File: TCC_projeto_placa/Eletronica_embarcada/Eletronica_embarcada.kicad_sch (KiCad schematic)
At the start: 70 parts, among them J1 ST-LINK, J2 OUT_Bluepill, J3 BOOT_JUMPER, J4 BUZZER

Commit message: ATT
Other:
- note added: "ACELERÔMETRO"
- note added: "MAGNETÔMETRO"
- moved on the sheet: C1, C2, C3, C4, C6, C7, C8, C?, CON?, D?, J1, J2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

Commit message: att
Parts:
- removed C?: C, symbol Device:C
- removed C?: 100nF, Capacitor_SMD:C_0603_1608Metric_Pad1.08x0.95mm_HandSolder, symbol Device:C
- removed CON?: USB_B, Connector_USB:USB_B_Lumberg_2411_02_Horizontal, symbol Connector:USB_B
- removed J1: ST-LINK, symbol Connector_Generic:Conn_02x05_Odd_Even
- removed J2: OUT_Bluepill, symbol Connector_Generic:Conn_01x04
- removed L?: BLM21PG221SN1D, Inductor_SMD:L_0805_2012Metric, symbol pspice:INDUCTOR
- added C? (x2): 0.1uF, symbol Device:C
- added C?: C, symbol Device:C
- added C?: 470u, 16V, symbol Device:C
- added C?: 100n, symbol Device:C
- added C?: 0.01uF, symbol Device:C
- added C?: 1000u,16V, symbol Device:C
- added C?: 2200pF, symbol Device:C
- added D? (x2): LED, symbol Device:LED
- added D?: D, Diode_SMD:D_SOD-123, symbol pspice:DIODE
- added J?: OUT_Bluepill, symbol Connector_Generic:Conn_01x04
- added J?: USB Conector, symbol Connector_Generic:Conn_01x05
- added J?: BM280 I2C, symbol Connector_Generic:Conn_01x06
- added J?: MPU6050, symbol Connector_Generic:Conn_01x08
- added R? (x3): 4.7k, symbol Device:R
- added R?: 510R, symbol Device:R
- added R? (x2): 10K, Resistor_SMD:R_0603_1608Metric_Pad0.98x0.95mm_HandSolder, symbol Device:R
- added R?: 510, symbol Device:R
- added U?: MPU-6050, Sensor_Motion:InvenSense_QFN-24_4x4mm_P0.5mm, symbol Sensor_Motion:MPU-6050
- added U?: NCP1117-5.0_SOT223, Package_TO_SOT_SMD:SOT-223-3_TabPin2, symbol Regulator_Linear:NCP1117-5.0_SOT223
- C3, C4: value 12p -> 20p
- C7, C8: value 100p -> 20p
- CON?: value CR123A -> Bateria min 7V
- Q? (x2): value Q_NPN_Darlington_BCE -> MMBT6427-F
- R?: value R -> 4.7k
- R? (x2): value R -> 20R
- R? (x2): value 1K -> 10K
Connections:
- net +3V3: now also U?.6 (VDDIO), C?.1, J?.1 (Pin_1), J?.1 (Pin_1), J?.1 (Pin_1), R?.1, R?.1, R?.1; no longer R?.1
- net +5V: now also R?.1, C?.1, C?.1, J?.1 (Pin_1), U?.2 (VO); no longer C?.1, D?.2 (A), J?.2 (Pin_2), J?.2 (Pin_2), RT?.2
- net 0: now also C?.2, C?.2, C?.2, C?.2, C?.2, C?.2, C?.2, C?.2, J?.2 (Pin_2), J?.2 (Pin_2), J?.4 (Pin_4), J?.4 (Pin_4), J?.5 (Pin_5), R?.2, R?.2, U?.1 (CLKIN), U?.1 (GND), U?.11 (FSYNC), U?.18 (GND)
- net D+: now also U?.15 (USBD+), J?.3 (Pin_3)
- net D-: now also U?.16 (USBD-), J?.2 (Pin_2)
- net PIN-SCL: now also J?.3 (Pin_3)
- net PIN-SDA: now also J?.4 (Pin_4)
- net SWCLK: now also J?.3 (Pin_3)
- net SWDIO: now also J?.2 (Pin_2)
- net PC13: now reaches U?.2 (PC13)
- net PC13: now also D?.1 (K)
- net at R?.1, U?.32 (PA11): now also R?.2
- net at R?.1, U?.33 (PA12): no longer R?.2
- net at U?.5 (SDO): now also R?.1
- net VDDIO: no longer names the net of U?.2 (CSB)
- net VDDIO: now also R?.2; no longer U?.6 (VDDIO)
- new net: C?.1, U?.10 (REGOUT)
- new net: C?.1, U?.20 (CPOUT)
- new net: R?.1, U?.9 (AD0)
- new net: D?.2 (A), R?.2 (x2)
- new net: C?.1, D?.2 (A), U?.3 (VI)
- new net +3.3V: C?.1, C?.1, R?.1, R?.1, U?.13 (VDD), U?.8 (VDDIO)
- new net GND: D?.1 (K)
- new net SCL1: J?.3 (Pin_3), R?.2, U?.23 (SCL)
- new net SDA1: J?.4 (Pin_4), R?.2, U?.24 (SDA)
- new net VBAT: C?.1, D?.1 (K), D?.2 (A), J?.2 (Pin_2), J?.2 (Pin_2), RT?.2
- no-connect marks 19 -> 23
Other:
- note added: "Alimentação"
- note added: "CIRCUITO ARM-M3"
- note added: "CONECTOR BOOT"
- note added: "CONECTORES PINOS DO BLUEPILL"
- note added: "Comunicação serial/USB"
- note added: "GRAVAÇÃO BLUEPILL STLINK"
- note added: "LED STATUS FOGUETE"
- note added: "USB CONECTOR"
- note removed: "Alimentação e comunicação/gravação FTDI"
- note removed: "LED STATUS"
- note removed: "MAGNETÔMETRO"
- moved on the sheet: C1, C2, C3, C4, C6, C7, C8, C?, CON?, D?, J3, J4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

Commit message: att
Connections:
- net PC13 is gone; now on net C13: D?.1 (K), U?.2 (PC13)
- net PIN-SCL is gone; now on net B10: J?.3 (Pin_3), R?.2, U?.4 (SCK)
- net PIN-SDA is gone; now on net B11: J?.4 (Pin_4), R?.2, U?.3 (SDI)
- net SCL1 is gone; now on net B6: J?.3 (Pin_3), R?.2, U?.23 (SCL)
- net SDA1 is gone; now on net B7: J?.4 (Pin_4), R?.2, U?.24 (SDA)
- net +3V3: now also C?.1, U?.17 (3V3OUT)
- net +5V: now also U?.4 (VCCIO)
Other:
- moved on the sheet: C6, D?, R2, R?, SW?

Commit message: att
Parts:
- added D?: D, Diode_SMD:D_SOD-123, symbol pspice:DIODE
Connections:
- net +5V: now also D?.1 (K); no longer C?.1, R?.1, U?.1 (IN), U?.3 (EN)
- new net: C?.1, D?.2 (A), R?.1, U?.1 (IN), U?.3 (EN)
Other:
- moved on the sheet: D?
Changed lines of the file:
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@@
   (junction (at 210.058 253.5936) (diameter 0) (color 0 0 0 0)
   )
-  (junction (at 208.0768 226.4918) (diameter 0) (color 0 0 0 0)
-  )
   (no_connect (at 341.7824 220.8022))
   (no_connect (at 382.4224 203.0222))
@@
     (stroke (width 0) (type default) (color 0 0 0 0))
   )
+  (wire (pts (xy 200.6854 218.44) (xy 212.09 218.44))
+    (stroke (width 0) (type default) (color 0 0 0 0))
+  )
   (wire (pts (xy 154.3558 42.3164) (xy 154.3558 43.2054))
     (stroke (width 0) (type default) (color 0 0 0 0))
@@
     (stroke (width 0) (type default) (color 0 0 0 0))
   )
-  (wire (pts (xy 208.0768 218.9226) (xy 208.0768 226.4918))
+  (wire (pts (xy 184.6834 226.4918) (xy 186.9694 226.4918))
     (stroke (width 0) (type default) (color 0 0 0 0))
   )
-  (wire (pts (xy 184.6834 226.4918) (xy 186.9694 226.4918))
+  (wire (pts (xy 200.6854 218.44) (xy 200.6854 226.4918))
     (stroke (width 0) (type default) (color 0 0 0 0))
   )
@@
     (stroke (width 0) (type default) (color 0 0 0 0))
   )
+  (wire (pts (xy 195.4276 253.619) (xy 199.0852 253.5936))
+    (stroke (width 0) (type default) (color 0 0 0 0))
+  )
   (wire (pts (xy 236.982 71.12) (xy 238.76 71.12))
     (stroke (width 0) (type default) (color 0 0 0 0))
@@
     (stroke (width 0) (type default) (color 0 0 0 0))
   )
-  (wire (pts (xy 227.3046 226.4918) (xy 230.7336 226.4918))
+  (wire (pts (xy 220.3958 226.4664) (xy 230.7336 226.4918))
     (stroke (width 0) (type default) (color 0 0 0 0))
   )
@@
     (stroke (width 0) (type default) (color 0 0 0 0))
   )
+  (wire (pts (xy 185.2676 253.619) (xy 182.6768 253.619))
+    (stroke (width 0) (type default) (color 0 0 0 0))
+  )
   (wire (pts (xy 40.4876 239.7252) (xy 49.8856 239.7252))
     (stroke (width 0) (type default) (color 0 0 0 0))
@@
     (stroke (width 0) (type default) (color 0 0 0 0))
   )
+  (wire (pts (xy 182.6768 253.619) (xy 182.6768 249.5804))
+    (stroke (width 0) (type default) (color 0 0 0 0))
+  )
   (wire (pts (xy 277.876 34.798) (xy 277.876 37.084))
     (stroke (width 0) (type default) (color 0 0 0 0))
@@
     (stroke (width 0) (type default) (color 0 0 0 0))
   )
-  (wire (pts (xy 208.0768 226.4918) (xy 217.1446 226.4918))
+  (wire (pts (xy 200.6854 226.4918) (xy 210.2358 226.4664))
     (stroke (width 0) (type default) (color 0 0 0 0))
   )
@@
     (stroke (width 0) (type default) (color 0 0 0 0))
   )
-  (wire (pts (xy 199.0852 251.5616) (xy 199.0852 253.5936))
-    (stroke (width 0) (type default) (color 0 0 0 0))
-  )
   (wire (pts (xy 93.5736 222.4532) (xy 93.5736 226.0092))
     (stroke (width 0) (type default) (color 0 0 0 0))
@@
     (stroke (width 0) (type default) (color 0 0 0 0))
   )
-  (wire (pts (xy 200.6854 226.4918) (xy 208.0768 226.4918))
-    (stroke (width 0) (type default) (color 0 0 0 0))
-  )
   (polyline (pts (xy 302.7934 171.3484) (xy 302.7934 244.094))
     (stroke (width 0) (type default) (color 0 0 0 0))
@@
     (effects (font (size 1.27 1.27)) (justify left bottom))
   )
-  (text "Alimentação" (at 178.5366 204.1398 0)
+  (text "Alimentação" (at 166.5732 202.4888 0)
     (effects (font (size 1.27 1.27)) (justify left bottom))
   )
@@
     )
   )
-  (global_label "VBAT" (shape input) (at 208.0768 218.9226 0) (fields_autoplaced)
+  (global_label "VBAT" (shape input) (at 212.09 218.44 0) (fields_autoplaced)
     (effects (font (size 1.27 1.27)) (justify left))
-    (property "Intersheet References" "${INTERSHEET_REFS}" (id 0) (at 214.8158 218.8432 0)
+    (property "Intersheet References" "${INTERSHEET_REFS}" (id 0) (at 218.829 218.3606 0)
       (effects (font (size 1.27 1.27)) (justify left) hide)
     )
@@
     )
   )
+  (global_label "LED2_status" (shape input) (at 305.5366 47.371 0) (fields_autoplaced)
+    (effects (font (size 1.27 1.27)) (justify left))
+    (property "Intersheet References" "${INTERSHEET_REFS}" (id 0) (at 319.3797 47.2916 0)
+      (effects (font (size 1.27 1.27)) (justify left) hide)
+    )
+  )
   (global_label "B11" (shape input) (at 359.41 69.85 0) (fields_autoplaced)
     (effects (font (size 1.27 1.27)) (justify left))
@@
     )
   )
+  (global_label "Pin_BUZZER" (shape input) (at 305.4096 50.6984 0) (fields_autoplaced)
+    (effects (font (size 1.27 1.27)) (justify left))
+    (property "Intersheet References" "${INTERSHEET_REFS}" (id 0) (at 319.2527 50.7778 0)
+      (effects (font (size 1.27 1.27)) (justify left) hide)
+    )
+  )
   (global_label "B7" (shape input) (at 382.27 44.45 180) (fields_autoplaced)
     (effects (font (size 1.27 1.27)) (justify right))
@@
     )
   )
+  (global_label "LED1_status" (shape input) (at 305.5874 43.8912 0) (fields_autoplaced)
+    (effects (font (size 1.27 1.27)) (justify left))
+    (property "Intersheet References" "${INTERSHEET_REFS}" (id 0) (at 319.4305 43.8118 0)
+      (effects (font (size 1.27 1.27)) (justify left) hide)
+    )
+  )
   (global_label "BOOT0" (shape input) (at 362.3564 146.5326 180) (fields_autoplaced)
     (effects (font (size 1.27 1.27)) (justify right))
@@
     (pin "2")
   )
+  (symbol (lib_name "+5V_2") (lib_id "power:+5V") (at 182.6768 249.5804 0) (unit 1)
+    (in_bom yes) (on_board yes) (fields_autoplaced)
+    (property "Reference" "#PWR?" (id 0) (at 182.6768 253.3904 0)
+      (effects (font (size 1.27 1.27)) hide)
+    )
+    (property "Value" "+5V" (id 1) (at 182.6768 244.7798 0))
+    (property "Footprint" "" (id 2) (at 182.6768 249.5804 0)
+      (effects (font (size 1.27 1.27)) hide)
+    )
+    (property "Datasheet" "" (id 3) (at 182.6768 249.5804 0)
+      (effects (font (size 1.27 1.27)) hide)
+    )
+    (pin "1")
+  )
   (symbol (lib_id "Device:C") (at 226.3394 178.8668 0) (mirror y) (unit 1)
     (in_bom yes) (on_board yes)
@@
     (pin "2")
   )
-  (symbol (lib_id "power:+5V") (at 199.0852 251.5616 0) (unit 1)
-    (in_bom yes) (on_board yes) (fields_autoplaced)
-    (property "Reference" "#PWR?" (id 0) (at 199.0852 255.3716 0)
-      (effects (font (size 1.27 1.27)) hide)
-    )
-    (property "Value" "+5V" (id 1) (at 199.0852 246.4816 0))
-    (property "Footprint" "" (id 2) (at 199.0852 251.5616 0)
-      (effects (font (size 1.27 1.27)) hide)
-    )
-    (property "Datasheet" "" (id 3) (at 199.0852 251.5616 0)
-      (effects (font (size 1.27 1.27)) hide)
-    )
-    (pin "1")
-  )
   (symbol (lib_id "pspice:0") (at 243.2558 234.1118 0) (unit 1)
     (in_bom yes) (on_board yes)
@@
   (symbol (lib_id "Device:Battery") (at 179.6034 226.4918 270) (unit 1)
     (in_bom yes) (on_board yes)
-    (property "Reference" "CON?" (id 0) (at 178.943 219.1512 90))
-    (property "Value" "Bateria min 7V" (id 1) (at 178.5874 221.742 90))
+    (property "Reference" "CON?" (id 0) (at 179.2986 230.2256 90))
+    (property "Value" "Bateria min 7V" (id 1) (at 174.117 222.885 90))
     (property "Footprint" "bt1:BAT_BH123A" (id 2) (at 181.1274 226.4918 90)
       (effects (font (size 1.27 1.27)) hide)
@@
     (pin "1")
   )
-  (symbol (lib_id "pspice:DIODE") (at 222.2246 226.4918 0) (unit 1)
+  (symbol (lib_id "pspice:DIODE") (at 215.3158 226.4664 0) (unit 1)
     (in_bom yes) (on_board yes)
-    (property "Reference" "D?" (id 0) (at 218.694 223.6216 0))
-    (property "Value" "D" (id 1) (at 218.4146 228.5238 0))
-    (property "Footprint" "Diode_SMD:D_SOD-123" (id 2) (at 222.2246 226.4918 0)
+    (property "Reference" "D?" (id 0) (at 211.7852 223.5962 0))
+    (property "Value" "D" (id 1) (at 211.5058 228.4984 0))
+    (property "Footprint" "Diode_SMD:D_SOD-123" (id 2) (at 215.3158 226.4664 0)
       (effects (font (size 1.27 1.27)) hide)
     )
-    (property "Datasheet" "~" (id 3) (at 222.2246 226.4918 0)
+    (property "Datasheet" "~" (id 3) (at 215.3158 226.4664 0)
       (effects (font (size 1.27 1.27)) hide)
     )
@@
     (pin "2")
   )
+  (symbol (lib_id "pspice:DIODE") (at 190.3476 253.619 0) (unit 1)
+    (in_bom yes) (on_board yes)
+    (property "Reference" "D?" (id 0) (at 190.5508 250.063 0))
+    (property "Value" "D" (id 1) (at 190.2968 257.7846 0))
+    (property "Footprint" "Diode_SMD:D_SOD-123" (id 2) (at 190.3476 253.619 0)
+      (effects (font (size 1.27 1.27)) hide)
+    )
+    (property "Datasheet" "~" (id 3) (at 190.3476 253.619 0)
+      (effects (font (size 1.27 1.27)) hide)
+    )
+    (pin "1")
+    (pin "2")
+  )
   (symbol (lib_id "Switch:SW_Push") (at 166.0398 49.0474 270) (unit 1)
     (in_bom yes) (on_board yes) (fields_autoplaced)
@@
   (symbol (lib_id "Device:Thermistor") (at 192.0494 226.4918 90) (unit 1)
     (in_bom yes) (on_board yes)
-    (property "Reference" "RT?" (id 0) (at 191.3382 220.5482 90))
-    (property "Value" "300mA - 304N" (id 1) (at 197.0024 223.2152 90))
+    (property "Reference" "RT?" (id 0) (at 192.024 229.3366 90))
+    (property "Value" "300mA - 304N" (id 1) (at 192.5066 223.1136 90))
     (property "Footprint" "Resistor_SMD:R_1812_4532Metric" (id 2) (at 192.0494 226.4918 0)
       (effects (font (size 1.27 1.27)) hide)
@@
       (reference "#PWR?") (unit 1) (value "+3.3V") (footprint "")
     )
+    (path "/267a1be8-190d-49cc-aee2-df8aa36b68cb"
+      (reference "#PWR?") (unit 1) (value "+5V") (footprint "")
+    )
     (path "/29420f44-f5f6-49c5-b8d5-a14b642ba274"
       (reference "#PWR?") (unit 1) (value "+3.3V") (footprint "")
     )
-    (path "/31152b0a-6f36-4fd2-9dac-c9c4592bc281"
-      (reference "#PWR?") (unit 1) (value "+5V") (footprint "")
-    )
     (path "/3331e586-f6dd-45c0-ba0d-38deff927543"
       (reference "#PWR?") (unit 1) (value "+3.3V") (footprint "")
@@
       (reference "D?") (unit 1) (value "D") (footprint "Diode_SMD:D_SOD-123")
     )
+    (path "/79017661-82ef-4398-b5a5-d73379b59701"
+      (reference "D?") (unit 1) (value "D") (footprint "Diode_SMD:D_SOD-123")
+    )

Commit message: att
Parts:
- removed C?: 1uF, Capacitor_SMD:C_0603_1608Metric_Pad1.08x0.95mm_HandSolder, symbol Device:C
- removed C?: 10nF, Capacitor_SMD:C_0603_1608Metric_Pad1.08x0.95mm_HandSolder, symbol Device:C
- removed C?: 4,7uF, Capacitor_SMD:C_0603_1608Metric_Pad1.08x0.95mm_HandSolder, symbol Device:C
- removed U?: FT232RL, Package_SO:SSOP-28_5.3x10.2mm_P0.65mm, symbol Interface_USB:FT232RL
- U?: value STM32F103C8Tx -> STM32F103CBT6
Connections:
- net +5V: no longer R?.1
- net B10: no longer J?.3 (Pin_3), R?.2, U?.21 (PB10), U?.4 (SCK)
- net B11: no longer J?.4 (Pin_4), R?.2, U?.22 (PB11), U?.3 (SDI)
- net B12: no longer U?.1 (*S), U?.25 (PB12)
- net B13: no longer C?.1, U?.26 (PB13), U?.6 (C)
- net B14: no longer U?.2 (Q), U?.27 (PB14)
- net B15: no longer U?.28 (PB15), U?.5 (D)
- net B6: no longer J?.3 (Pin_3), R?.2, U?.23 (SCL), U?.42 (PB6)
- net B7: no longer J?.4 (Pin_4), R?.2, U?.24 (SDA), U?.43 (PB7)
- net B8: no longer U?.45 (PB8)
- net B9: no longer U?.46 (PB9)
- net LED1_status: now also U?.45 (PB8)
- net LED2_status: now also U?.46 (PB9)
- new net +5VD: R?.1
- new net B10_BAR: J?.3 (Pin_3), R?.2, U?.21 (PB10), U?.4 (SCK)
- new net B11_BAR: J?.4 (Pin_4), R?.2, U?.22 (PB11), U?.3 (SDI)
- new net B12_MEM: U?.1 (*S), U?.25 (PB12)
- new net B13_MEM: C?.1, U?.26 (PB13), U?.6 (C)
- new net B14_MEM: U?.2 (Q), U?.27 (PB14)
- new net B15_MEM: U?.28 (PB15), U?.5 (D)
- new net B6_ACCE: J?.3 (Pin_3), R?.2, U?.23 (SCL), U?.42 (PB6)
- new net B7_ACCE: J?.4 (Pin_4), R?.2, U?.24 (SDA), U?.43 (PB7)
- no-connect marks 23 -> 9
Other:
- note removed: "Comunicação serial/USB"
- moved on the sheet: C8, C?, R?, U?

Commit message: aat
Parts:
- LED?: value BLUE -> Power ON
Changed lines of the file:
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@@
       (effects (font (size 1.27 1.27)) (justify right))
     )
-    (property "Value" "BLUE" (id 1) (at 196.2912 265.5316 90)
+    (property "Value" "Power ON" (id 1) (at 196.2912 265.5316 90)
       (effects (font (size 1.27 1.27)) (justify right))
     )
@@
     )
     (path "/3eb2af48-db14-40c5-89b2-80d6417d5ec9"
-      (reference "LED?") (unit 1) (value "BLUE") (footprint "LED_SMD:LED_0603_1608Metric_Pad1.05x0.95mm_HandSolder")
+      (reference "LED?") (unit 1) (value "Power ON") (footprint "LED_SMD:LED_0603_1608Metric_Pad1.05x0.95mm_HandSolder")
     )
     (path "/0e72554a-372c-4459-91eb-e0cbd9668bdb"

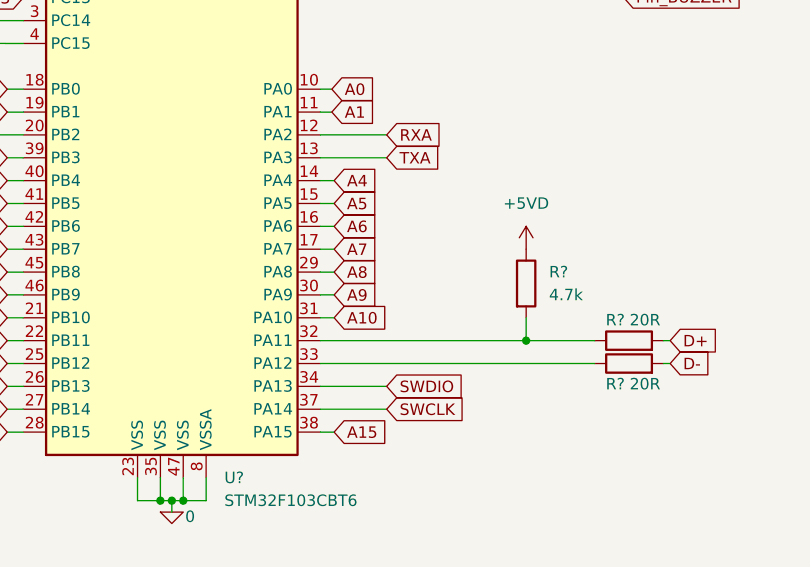
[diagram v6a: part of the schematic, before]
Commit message: atualizado com botao pra gravação e EMA
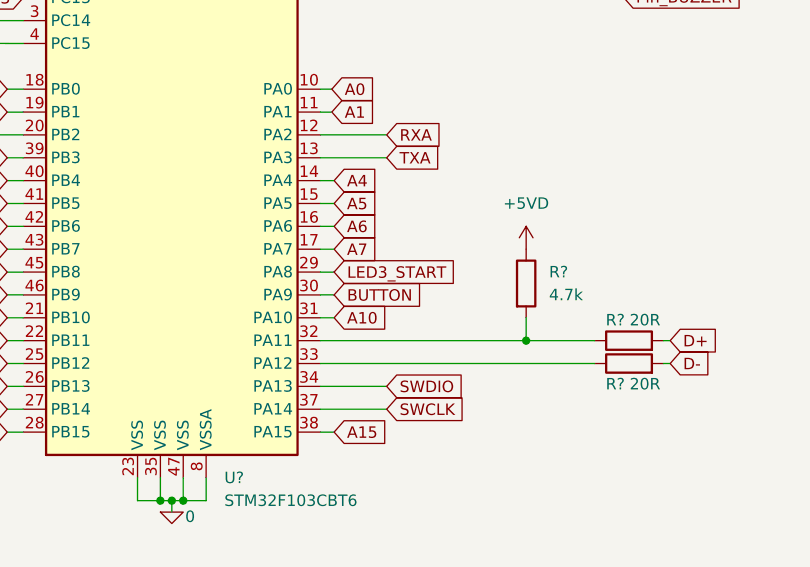
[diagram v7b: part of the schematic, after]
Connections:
- net A8: no longer U?.29 (PA8)
- net A9: no longer U?.30 (PA9)
- new net BUTTON: U?.30 (PA9)
- new net LED3_START: U?.29 (PA8)
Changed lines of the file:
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@@
     )
   )
-  (global_label "A8" (shape input) (at 273.304 81.28 0) (fields_autoplaced)
+  (global_label "LED3_START" (shape input) (at 273.304 81.28 0) (fields_autoplaced)
     (effects (font (size 1.27 1.27)) (justify left))
-    (property "Intersheet References" "${INTERSHEET_REFS}" (id 0) (at 278.0152 81.2006 0)
+    (property "Intersheet References" "${INTERSHEET_REFS}" (id 0) (at 286.8447 81.2006 0)
       (effects (font (size 1.27 1.27)) (justify left) hide)
     )
@@
     )
   )
-  (global_label "A9" (shape input) (at 273.304 83.82 0) (fields_autoplaced)
+  (global_label "BUTTON" (shape input) (at 273.304 83.82 0) (fields_autoplaced)
     (effects (font (size 1.27 1.27)) (justify left))
-    (property "Intersheet References" "${INTERSHEET_REFS}" (id 0) (at 278.0152 83.7406 0)
+    (property "Intersheet References" "${INTERSHEET_REFS}" (id 0) (at 282.9138 83.7406 0)
       (effects (font (size 1.27 1.27)) (justify left) hide)
     )

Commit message: att
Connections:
- net A1: no longer U?.11 (PA1)
- net Pin_BUZZER: now also U?.11 (PA1)
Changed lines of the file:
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@@
-    )
-  )
-  (global_label "LED2_status" (shape input) (at 305.5366 47.371 0) (fields_autoplaced)
-    (effects (font (size 1.27 1.27)) (justify left))
-    (property "Intersheet References" "${INTERSHEET_REFS}" (id 0) (at 319.3797 47.2916 0)
-      (effects (font (size 1.27 1.27)) (justify left) hide)
     )
   )
@@
     )
   )
-  (global_label "A1" (shape input) (at 273.05 63.5 0) (fields_autoplaced)
-    (effects (font (size 1.27 1.27)) (justify left))
-    (property "Intersheet References" "${INTERSHEET_REFS}" (id 0) (at 277.7612 63.4206 0)
-      (effects (font (size 1.27 1.27)) (justify left) hide)
-    )
-  )
   (global_label "Reset" (shape input) (at 150.5458 43.2054 180) (fields_autoplaced)
     (effects (font (size 1.27 1.27)) (justify right))
@@
     )
   )
-  (global_label "Pin_BUZZER" (shape input) (at 305.4096 50.6984 0) (fields_autoplaced)
-    (effects (font (size 1.27 1.27)) (justify left))
-    (property "Intersheet References" "${INTERSHEET_REFS}" (id 0) (at 319.2527 50.7778 0)
-      (effects (font (size 1.27 1.27)) (justify left) hide)
-    )
-  )
   (global_label "B7" (shape input) (at 382.27 44.45 180) (fields_autoplaced)
     (effects (font (size 1.27 1.27)) (justify right))
@@
     )
   )
-  (global_label "LED1_status" (shape input) (at 305.5874 43.8912 0) (fields_autoplaced)
-    (effects (font (size 1.27 1.27)) (justify left))
-    (property "Intersheet References" "${INTERSHEET_REFS}" (id 0) (at 319.4305 43.8118 0)
-      (effects (font (size 1.27 1.27)) (justify left) hide)
-    )
-  )
   (global_label "BOOT0" (shape input) (at 362.3564 146.5326 180) (fields_autoplaced)
     (effects (font (size 1.27 1.27)) (justify right))
@@
     )
   )
+  (global_label "Pin_BUZZER" (shape input) (at 273.05 63.5 0) (fields_autoplaced)
+    (effects (font (size 1.27 1.27)) (justify left))
+    (property "Intersheet References" "${INTERSHEET_REFS}" (id 0) (at 286.8931 63.5794 0)
+      (effects (font (size 1.27 1.27)) (justify left) hide)
+    )
+  )
